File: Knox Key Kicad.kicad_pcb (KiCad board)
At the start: 2 copper layers, 27.2 x 17.1 mm, 29 parts, among them J3 Conn_01x05, P1 USB_C_Plug_USB2.0, SW1 SW_Push, U2 ATECC608B-MAHDA, U3 MCP1700x-330xxTT, U4 USBLC6-2SC6, U6 STM32L433CBTx, Y1 8MHz

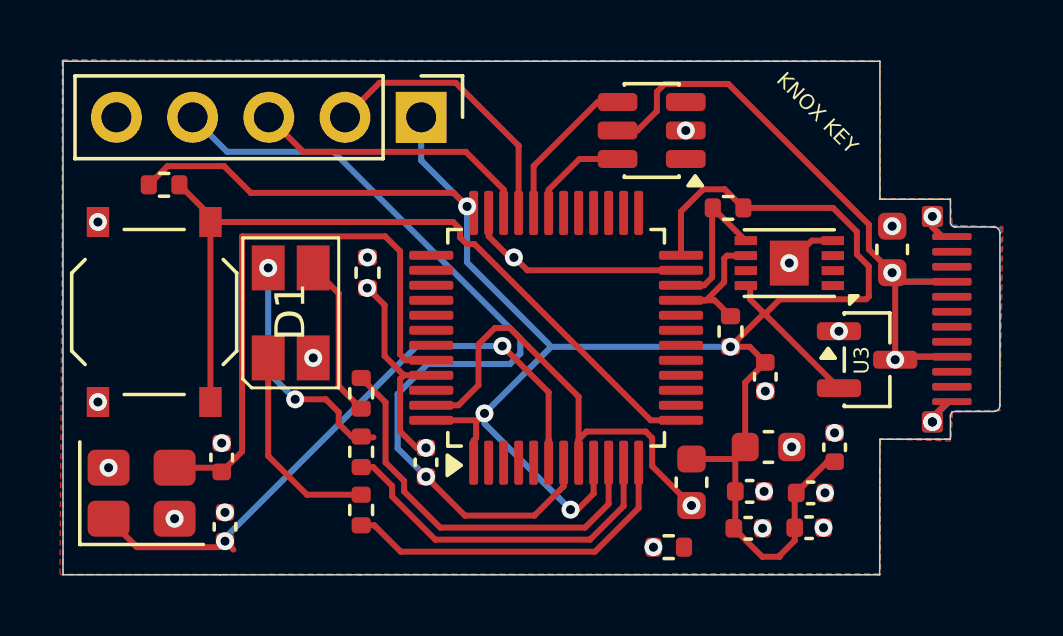
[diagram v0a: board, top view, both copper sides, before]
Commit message: docs: add project journal, map screenshots, and update firmware code/configs
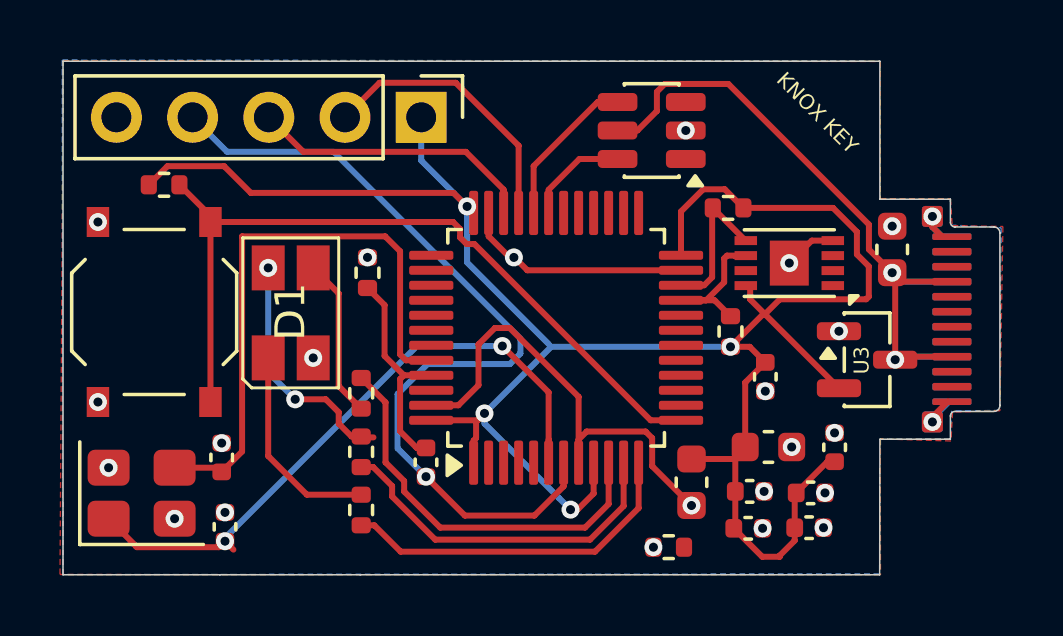
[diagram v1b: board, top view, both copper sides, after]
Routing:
- net GND: vias 25 -> 24
- net /BOOT0: vias 2 -> 0
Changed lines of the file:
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@@
-	)
-	(via
-		(at 174.95 112.185)
-		(size 0.6)
-		(drill 0.3)
-		(layers "F.Cu" "B.Cu")
-		(locked yes)
-		(net 3)
 	)
 	(via
@@
 		(net 4)
 	)
-	(via
-		(at 156.11 107.720001)
-		(size 0.6)
-		(drill 0.3)
-		(layers "F.Cu" "B.Cu")
-		(locked yes)
-		(net 4)
-	)
-	(via
-		(at 158.07 113.050001)
-		(size 0.6)
-		(drill 0.3)
-		(layers "F.Cu" "B.Cu")
-		(locked yes)
-		(net 4)
-	)
